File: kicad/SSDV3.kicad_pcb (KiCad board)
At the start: 4 copper layers, 58.4 x 28.8 mm, 54 parts, among them J1 XT30PW-M, J2 XT30PW-F, J3 SolderPad_1x02, J4 SolderPad_1x03, Q1 CSD19537Q3, Q2 BSZ096N10LS5, U1 LM5146

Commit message: FET Optimizations
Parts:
- removed G*** (x2): LOGO, LOGO
- added C19: 22uF, Capacitor_SMD:C_1206_3216Metric, F.Cu at (149.1, 103.6)
- added C20: 22uF, Capacitor_SMD:C_1206_3216Metric, F.Cu at (146.7, 103.6)
- added C21: 22uF, Capacitor_SMD:C_1206_3216Metric, F.Cu at (144.3, 103.6)
- added C22: 22uF, Capacitor_SMD:C_1206_3216Metric, F.Cu at (141.9, 103.6)
- added C23: 22uF, Capacitor_SMD:C_1206_3216Metric, F.Cu at (139.5, 103.6)
- added C24: 100uF, Capacitor_Tantalum_SMD:CP_EIA-7343-20_Kemet-V_HandSolder, F.Cu at (135.5, 111.5)
- added HS1: 241802B92200G, Heatsink_JJ:24180xB9x200G, B.Cu at (155.5, 111.5)
- added SW1: SW_SP3T, Button_Switch_SMD:SW_SP3T_PCM13, F.Cu at (171.0, 128.0)
- C1: value 100nF -> 100uF; footprint Capacitor_SMD:C_0603_1608Metric -> Connector_Wire:SolderWire-0.5sqmm_1x02_P4.6mm_D0.9mm_OD2.1mm
- C10, C11: value 2.2nF -> 100nF
- C12: value 10pF -> 2.2uF; footprint Capacitor_SMD:C_0603_1608Metric -> Capacitor_SMD:C_0805_2012Metric
- C13: value 22uF -> 47nF; footprint Capacitor_SMD:C_1210_3225Metric -> Capacitor_SMD:C_0603_1608Metric
- C14, C15: value 22uF -> 2.2nF; footprint Capacitor_SMD:C_1210_3225Metric -> Capacitor_SMD:C_0603_1608Metric
- C16: value 22uF -> 10pF; footprint Capacitor_SMD:C_1210_3225Metric -> Capacitor_SMD:C_0603_1608Metric
- C17: value 100uF -> 100nF; footprint Capacitor_Tantalum_SMD:CP_EIA-7343-20_Kemet-V_HandSolder -> Capacitor_SMD:C_0603_1608Metric
- C18: value 100uF -> 12pF; footprint Capacitor_Tantalum_SMD:CP_EIA-7343-20_Kemet-V_HandSolder -> Capacitor_SMD:C_0603_1608Metric
- C2: value 10uF -> 100nF; footprint Capacitor_SMD:C_1210_3225Metric -> Capacitor_SMD:C_0603_1608Metric
- C3, C4: value 10uF -> 4.7uF; footprint Capacitor_SMD:C_1210_3225Metric -> Capacitor_SMD:C_1206_3216Metric
- C5, C8: value 100nF -> 4.7uF; footprint Capacitor_SMD:C_0603_1608Metric -> Capacitor_SMD:C_1206_3216Metric
- C6: value 2.2uF -> 4.7uF; footprint Capacitor_SMD:C_0805_2012Metric -> Capacitor_SMD:C_1206_3216Metric
- C7: value 47nF -> 4.7uF; footprint Capacitor_SMD:C_0603_1608Metric -> Capacitor_SMD:C_1206_3216Metric
- C9: value 12pF -> 100nF
- D1: value 1.5SMCxxA -> SMBJ64A; footprint Diode_SMD:D_SMC -> Diode_SMD:D_SMB; moved to F.Cu
- J1: value XT30PW-M -> XT30U-M; footprint Connector_AMASS:AMASS_XT30PW-M_1x02_P2.50mm_Horizontal -> Connector_AMASS:AMASS_XT30U-M_1x02_P5.0mm_Vertical; moved to B.Cu
- J2: value XT30PW-F -> XT30U-F; footprint Connector_AMASS:AMASS_XT30PW-F_1x02_P2.50mm_Horizontal -> Connector_AMASS:AMASS_XT30U-F_1x02_P5.0mm_Vertical; moved to B.Cu
- J3: value SolderPad_1x02 -> Conn_01x02_MountingPin; footprint Connector_Pad:SolderWirePad_1x02_SMD_1.5x2mm -> Connector_JST:JST_GH_SM02B-GHS-TB_1x02-1MP_P1.25mm_Horizontal; moved to F.Cu
- J4: value SolderPad_1x03 -> Conn_01x03_MountingPin; footprint Connector_Pad:SolderWirePad_1x03_SMD_1.5x2mm -> Connector_JST:JST_GH_SM03B-GHS-TB_1x03-1MP_P1.25mm_Horizontal
- JP1, JP2: moved to F.Cu
- L1: value 6.8uH -> 4.7uH; footprint Inductor_SMD:L_Vishay_IHLP-4040 -> Inductor_SMD:L_Bourns_SRP1038C_10.0x10.0mm
- Q1: value CSD19537Q3 -> BSZ146N10LS5ATMA1; footprint Package_SON_JJ:Texas_DQG0008A_3.3x3.3mm_P0.65mm_ThermalVias-D0.3mm -> Package_SON_JJ:Infineon_PG-TSDSON-8-26_3.3x3.3mm_P0.65mm_ThermalVias-D0.3mm
- Q2: value BSZ096N10LS5 -> BSZ146N10LS5ATMA1; footprint Package_SON_JJ:Infineon_PG-TSDSON-8-26_3.3x3.3mm_P0.65mm_ThermalVias-D0.3mm -> Package_SON_JJ:Infineon_PG-TSDSON-8-26_3.3x3.3mm_P0.65mm
- R1: value 150k -> 2.2
- R10: value 1k -> 6.8k
- R11: value 20k -> 6.81k
- R12: value 15k -> 3.48k
- R13: value 6.81k -> 3.74k
- R14: value 3.48k -> 2.2
- R15: value 3.74k -> 430
- R2: value 13k -> 150k
- R3: value 2.2 -> 13k
- R4: value 33k -> 20k
- R5: value 20k -> 24k
- R6: value 0 -> 20k
- R7: value 20k -> 0
- R8: value 2.2 -> 1k
- R9: value 430 -> 20k
- moved JP1 85.3 mm to (75.8, 142.3), turned to 0 degrees
- moved J4 84.1 mm to (78.3, 109.1)
- moved JP2 83.1 mm to (75.8, 145.8), turned to 0 degrees
- moved H2 79.8 mm to (92.2, 109.1), turned to 0 degrees
- moved H3 78.3 mm to (92.2, 111.5), turned to 0 degrees
- moved D3 63.1 mm to (101.7, 107.8)
- moved C1 57.5 mm to (99.5, 146.2), turned to 0 degrees
- moved D4 52.5 mm to (96.3, 107.1), turned to 0 degrees
- moved NT1 47.9 mm to (107.6, 130.4), turned to 0 degrees
- moved J3 44.6 mm to (187.8, 103.5), turned to 90 degrees
- moved R16 44.1 mm to (108.5, 128.2)
- moved D2 43.5 mm to (108.6, 125.2), turned to 0 degrees
- moved H1 36.0 mm to (92.2, 106.6), turned to 0 degrees
- moved C14 33.7 mm to (170.0, 113.8), turned to 180 degrees
- moved C16 29.9 mm to (165.8, 116.2), turned to -90 degrees
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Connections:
- C1 pad 1: /buck_converter/U1_VIN -> VIN
- C10 pad 1: /buck_converter/COMP_RC2 -> VIN
- C10 pad 2: /buck_converter/FB -> PGND
- C11 pad 1: /buck_converter/COMP -> VIN
- C11 pad 2: /buck_converter/COMP_RC1 -> PGND
- C12 pad 1: /buck_converter/FB -> VCC
- C12 pad 2: /buck_converter/COMP -> PGND
- C13 pad 1: VOUT -> /buck_converter/SS_TRK
- C13 pad 2: PGND -> AGND
- C14 pad 1: VOUT -> /buck_converter/COMP_RC2
- C14 pad 2: PGND -> /buck_converter/FB
- C15 pad 1: VOUT -> /buck_converter/COMP
- C15 pad 2: PGND -> /buck_converter/COMP_RC1
- C16 pad 1: VOUT -> /buck_converter/FB
- C16 pad 2: PGND -> /buck_converter/COMP
- C17 pad 1: VOUT -> /buck_converter/RBST
- C17 pad 2: PGND -> /buck_converter/BST
- C18 pad 1: VOUT -> /buck_converter/ILIM
- C2 pad 1: VIN -> /buck_converter/U1_VIN
- C6 pad 1: VCC -> VIN
- C7 pad 1: /buck_converter/SS_TRK -> VIN
- C7 pad 2: AGND -> PGND
- C8 pad 1: /buck_converter/RBST -> VIN
- C8 pad 2: /buck_converter/BST -> PGND
- C9 pad 1: /buck_converter/ILIM -> VIN
- Q1 pad 2: /buck_converter/SW -> /buck_converter/HO
- Q1 pad 3: /buck_converter/SW -> VIN
- R1 pad 2: U1_EN -> /buck_converter/U1_VIN
- R10 pad 1: VOUT -> /buck_converter/FB
- R10 pad 2: /buck_converter/COMP_RC2 -> /buck_converter/COMP_RC1
- R11 pad 1: VOUT -> /buck_converter/FB
- R11 pad 2: /buck_converter/FB -> /buck_converter/JP_CFG1
- R12 pad 2: /buck_converter/COMP_RC1 -> /buck_converter/JP_CFG2
- R13 pad 2: /buck_converter/JP_CFG1 -> AGND
- R14 pad 1: /buck_converter/FB -> /buck_converter/RBST
- R14 pad 2: /buck_converter/JP_CFG2 -> /buck_converter/SW
- R15 pad 1: /buck_converter/FB -> /buck_converter/SW
- R15 pad 2: AGND -> /buck_converter/ILIM
- R2 pad 1: U1_EN -> VIN
- R2 pad 2: AGND -> U1_EN
- R3 pad 1: VIN -> U1_EN
- R3 pad 2: /buck_converter/U1_VIN -> AGND
- R4 pad 1: /buck_converter/RT -> VCC
- R4 pad 2: AGND -> PG
- R5 pad 1: VCC -> /buck_converter/RT
- R5 pad 2: /buck_converter/SYNCIN -> AGND
- R6 pad 1: /buck_converter/SYNCIN -> VCC
- R6 pad 2: AGND -> /buck_converter/SYNCIN
- R7 pad 1: VCC -> /buck_converter/SYNCIN
- R7 pad 2: PG -> AGND
- R8 pad 1: /buck_converter/RBST -> VOUT
- R8 pad 2: /buck_converter/SW -> /buck_converter/COMP_RC2
- R9 pad 1: /buck_converter/SW -> VOUT
- R9 pad 2: /buck_converter/ILIM -> /buck_converter/FB
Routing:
- net PGND: track 25.1 -> 0.00 mm, vias 78 -> 0
- net U1_EN: track 19.1 -> 0.00 mm, vias 1 -> 0
- net VIN: track 17.5 -> 0.00 mm, vias 12 -> 0
- net VCC: track 17.1 -> 0.00 mm, vias 2 -> 0
- net AGND: track 16.6 -> 0.00 mm, vias 2 -> 0
- net /buck_converter/SW: track 19.4 -> 3.11 mm, vias 4 -> 1
- net /buck_converter/FB: track 15.6 -> 0.00 mm
- net /buck_converter/LO: track 15.0 -> 0.00 mm, vias 2 -> 0
- net PG: track 11.3 -> 0.00 mm
- net /buck_converter/COMP: track 5.55 -> 0.00 mm
- net /buck_converter/HO: track 6.61 -> 1.38 mm, vias 2 -> 1
- net /buck_converter/SYNCIN: track 4.41 -> 0.00 mm
- net VOUT: track 4.05 -> 0.00 mm, vias 1 -> 0
- net /buck_converter/U1_VIN: track 2.97 -> 0.00 mm
- net /buck_converter/ILIM: track 2.92 -> 0.00 mm
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- removed copper zone on F.Cu, net /buck_converter/HO
- removed copper zone on F.Cu, net /buck_converter/LO
- removed copper zone on B.Cu, net /buck_converter/SW
- removed copper zone on F.Cu, net /buck_converter/SW
- removed copper zone on In2.Cu, net /buck_converter/SW
- removed copper zone on F.Cu, net /buck_converter/U1_VIN
- removed copper zone on F.Cu, net AGND
- removed copper zone on B.Cu, net PGND
- removed copper zone on F.Cu, net PGND
- removed copper zone on In2.Cu, net PGND
- removed copper zone on B.Cu, net VIN
- removed copper zone on F.Cu, net VIN
- removed copper zone on In2.Cu, net VIN
- removed copper zone on B.Cu, net VOUT
- removed copper zone on F.Cu, net VOUT
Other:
- board size 58.4 x 28.8 mm -> 71 x 23 mm
- board text removed: "12V"
- board text removed: "5.1V"
- board text removed: "7.4V"
- board text removed: "9.6V"
- board text removed: "CAUTION HOT SURFACE"
- board text removed: "EN"
- board text removed: "GND"
- board text removed: "INPUT: 20-60V⎓4A OUTPUT: 5.1-12V⎓8A"
- board text removed: "JLCJLCJLCJLC"
- board text removed: "OFF"
- board text removed: "ON"
- board text removed: "OUTPUT CONFIG"
- board text removed: "PG"
- board text removed: "Prod 2545 Rev. D"
- board text removed: "Prod 2545 Rev. D Julian Joaquin"
- board text removed: "SSD"
- board text removed: "V1"
- board text removed: "V2"
- board text removed: "V3"
- board text removed: "VCC"

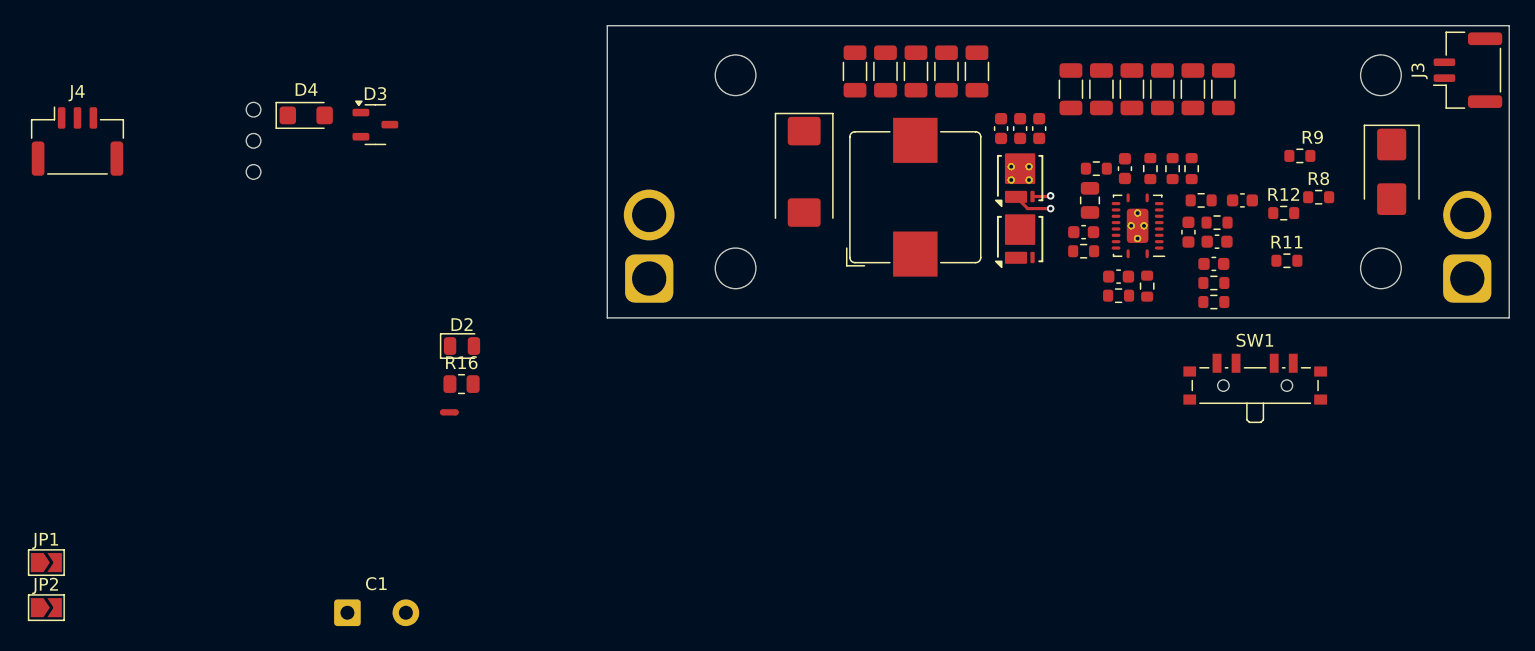
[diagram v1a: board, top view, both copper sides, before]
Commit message: Wrong design files initially commited
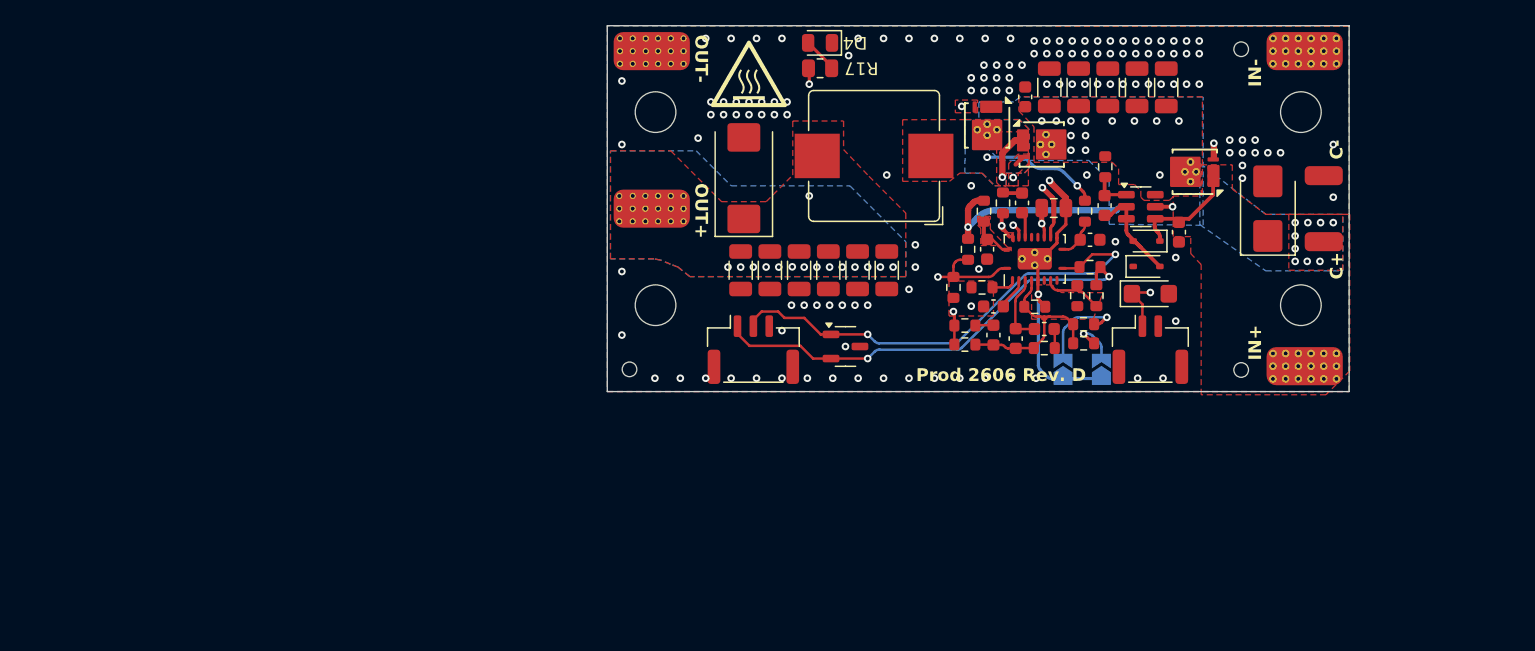
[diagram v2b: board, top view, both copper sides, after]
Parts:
- removed C1: 100uF, Connector_Wire:SolderWire-0.5sqmm_1x02_P4.6mm_D0.9mm_OD2.1mm
- removed SW1: SW_SP3T, Button_Switch_SMD:SW_SP3T_PCM13
- added D5: 60V, Diode_SMD:D_SMF, F.Cu at (162.8, 121.1)
- added D6: 8V, Package_TO_SOT_SMD:SOT-23-3, F.Cu at (138.8, 125.2)
- added G***: LOGO, LOGO, F.Cu at (131.1, 103.8)
- added G***: LOGO, LOGO, B.Cu at (146.5, 119.0)
- added J5: SolderPad, Connector_Wire:SolderWirePad_1x01_SMD_3x6mm, F.Cu at (123.5, 114.4)
- added J6: SolderPad, Connector_Wire:SolderWirePad_1x01_SMD_3x6mm, F.Cu at (123.5, 102.0)
- added J7: SM02B-GHS-TB(LF)(SN), Connector_JST:JST_GH_SM02B-GHS-TB_1x02-1MP_P1.25mm_Horizontal, F.Cu at (162.8, 125.5)
- added J8: SM03B-GHS-TB(LF)(SN), Connector_JST:JST_GH_SM03B-GHS-TB_1x03-1MP_P1.25mm_Horizontal, F.Cu at (131.5, 125.5)
- added Q3: BSZ146N10LS5, Package_SON_JJ:Infineon_PG-TSDSON-8-26_3.3x3.3mm_P0.65mm_ThermalVias-D0.3mm, F.Cu at (149.9, 107.8)
- added R17: 1k, Resistor_SMD:R_0805_2012Metric, F.Cu at (136.7, 103.3)
- added U2: LM5146, Package_QFN_JJ:Texas_RGY0020B_EP_3.5x4.5mm_P0.5mm_ThermalVias-D0.3mm, F.Cu at (153.6, 118.3)
- C11: value 100nF -> 2.2uF; footprint Capacitor_SMD:C_0603_1608Metric -> Capacitor_SMD:C_0805_2012Metric
- C12: value 2.2uF -> 47nF; footprint Capacitor_SMD:C_0805_2012Metric -> Capacitor_SMD:C_0603_1608Metric
- C13: value 47nF -> 100nF
- C14: value 2.2nF -> 8.2pF
- C15: value 2.2nF -> 1.5nF
- C16: value 10pF -> 4.7nF
- C17: value 100nF -> 68pF
- C18: value 12pF -> 22uF; footprint Capacitor_SMD:C_0603_1608Metric -> Capacitor_SMD:C_1206_3216Metric
- C3, C4: value 4.7uF -> 100nF; footprint Capacitor_SMD:C_1206_3216Metric -> Capacitor_SMD:C_0603_1608Metric
- C9: value 100nF -> 4.7uF; footprint Capacitor_SMD:C_0603_1608Metric -> Capacitor_SMD:C_1206_3216Metric
- D1: value SMBJ64A -> 64V
- D2: value GREEN -> BAT46WS; footprint LED_SMD:LED_0805_2012Metric -> Diode_SMD:D_SOD-323
- D3: value 8V -> BAT46WS; footprint Package_TO_SOT_SMD:SOT-23-3 -> Diode_SMD:D_SOD-323
- D4: value 60V -> GREEN; footprint Diode_SMD:D_SMF -> LED_SMD:LED_0805_2012Metric
- J1: value XT30U-M -> SolderPad; footprint Connector_AMASS:AMASS_XT30U-M_1x02_P5.0mm_Vertical -> Connector_Wire:SolderWirePad_1x01_SMD_3x6mm; moved to F.Cu
- J2: value XT30U-F -> SolderPad; footprint Connector_AMASS:AMASS_XT30U-F_1x02_P5.0mm_Vertical -> Connector_Wire:SolderWirePad_1x01_SMD_1.5x3mm; moved to F.Cu
- J3: value Conn_01x02_MountingPin -> SolderPad; footprint Connector_JST:JST_GH_SM02B-GHS-TB_1x02-1MP_P1.25mm_Horizontal -> Connector_Wire:SolderWirePad_1x01_SMD_1.5x3mm
- J4: value Conn_01x03_MountingPin -> SolderPad; footprint Connector_JST:JST_GH_SM03B-GHS-TB_1x03-1MP_P1.25mm_Horizontal -> Connector_Wire:SolderWirePad_1x01_SMD_3x6mm
- JP1, JP2: moved to B.Cu
- Q1: value BSZ146N10LS5ATMA1 -> BSZ146N10LS5
- Q2: value BSZ146N10LS5ATMA1 -> BSZ146N10LS5; footprint Package_SON_JJ:Infineon_PG-TSDSON-8-26_3.3x3.3mm_P0.65mm -> Package_SON_JJ:Infineon_PG-TSDSON-8-26_3.3x3.3mm_P0.65mm_ThermalVias-D0.3mm
- R1: value 2.2 -> 1.5k
- R10: value 6.8k -> 560
- R11: value 6.81k -> 1.5k
- R12: value 3.48k -> 20k
- R13: value 3.74k -> 10k
- R14: value 2.2 -> 6.81k
- R15: value 430 -> 3.48k
- R16: value 1k -> 3.74k; footprint Resistor_SMD:R_0805_2012Metric -> Resistor_SMD:R_0603_1608Metric
- R3: value 13k -> 12k
- R4, R9: value 20k -> 2.2
- R8: value 1k -> 20k
- U1: value LM5146 -> LM5050-1; footprint Package_QFN_JJ:Texas_RGY0020B_EP_3.5x4.5mm_P0.5mm_ThermalVias-D0.3mm -> Package_TO_SOT_SMD:TSOT-23-6
- moved J4 96.9 mm to (174.9, 102.0), turned to -90 degrees
- moved JP2 85.1 mm to (158.9, 127.0), turned to 90 degrees
- moved JP1 81.5 mm to (155.9, 127.0), turned to 90 degrees
- moved H2 79.8 mm to (169.9, 127.1), turned to 180 degrees
- moved H3 78.3 mm to (169.9, 101.8), turned to 180 degrees
- moved D3 61.7 mm to (162.4, 119.0)
- moved D2 54.5 mm to (162.4, 117.0), turned to 180 degrees
- moved J2 53.2 mm to (176.4, 117.0), turned to -90 degrees
- moved NT1 47.6 mm to (153.9, 119.4), turned to -90 degrees
- moved R16 45.5 mm to (153.6, 122.1)
- moved D4 40.9 mm to (136.7, 101.3), turned to 180 degrees
- moved H1 36.0 mm to (121.8, 127.0), turned to 180 degrees
- moved R12 27.2 mm to (148.1, 125.1)
- moved R11 25.9 mm to (148.1, 123.6)
- moved R9 23.7 mm to (151.1, 114.0), turned to -90 degrees
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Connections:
- C11 pad 1: VIN -> VCC
- C12 pad 1: VCC -> /buck_converter/SS_TRK
- C12 pad 2: PGND -> AGND
- C13 pad 1: /buck_converter/SS_TRK -> /buck_converter/RBST
- C13 pad 2: AGND -> /buck_converter/BST
- C14 pad 1: /buck_converter/COMP_RC2 -> /buck_converter/ILIM
- C14 pad 2: /buck_converter/FB -> PGND
- C15 pad 1: /buck_converter/COMP -> /buck_converter/COMP_RC2
- C15 pad 2: /buck_converter/COMP_RC1 -> /buck_converter/FB
- C16 pad 1: /buck_converter/FB -> /buck_converter/COMP
- C16 pad 2: /buck_converter/COMP -> /buck_converter/COMP_RC1
- C17 pad 1: /buck_converter/RBST -> /buck_converter/FB
- C17 pad 2: /buck_converter/BST -> /buck_converter/COMP
- C18 pad 1: /buck_converter/ILIM -> VOUT
- C2 pad 1: /buck_converter/U1_VIN -> VBAT
- C3 pad 1: VIN -> /rpp/U1_VS
- C3 pad 2: PGND -> /rpp/U1_GND
- C4 pad 1: VIN -> /buck_converter/U2_VIN
- D1 pad 1: VIN -> VBAT
- D2 pad 1: PGND -> VBAT
- D2 pad 2: /buck_converter/VOUT_LED -> /rpp/U1_GND
- D3 pad 1: PG -> PGND
- D3 pad 2: VCC -> /rpp/U1_GND
- D4 pad 1: U1_EN -> PGND
- D4 pad 2: PGND -> /buck_converter/VOUT_LED
- J1 pad 1: PGND -> VBAT
- J2 pad 1: PGND -> VIN
- J3 pad 1: U1_EN -> PGND
- J4 pad 1: VCC -> PGND
- Q1 pad 1: /buck_converter/SW -> VBAT
- Q1 pad 2: /buck_converter/HO -> /rpp/U1_GATE
- Q2 pad 1: PGND -> /buck_converter/SW
- Q2 pad 2: /buck_converter/LO -> /buck_converter/HO
- Q2 pad 3: /buck_converter/SW -> VIN
- R1 pad 2: /buck_converter/U1_VIN -> /rpp/U1_VS
- R10 pad 1: /buck_converter/FB -> /buck_converter/SW
- R10 pad 2: /buck_converter/COMP_RC1 -> /buck_converter/ILIM
- R11 pad 1: /buck_converter/FB -> VOUT
- R11 pad 2: /buck_converter/JP_CFG1 -> /buck_converter/COMP_RC2
- R12 pad 1: /buck_converter/FB -> VOUT
- R12 pad 2: /buck_converter/JP_CFG2 -> /buck_converter/FB
- R13 pad 2: AGND -> /buck_converter/COMP_RC1
- R14 pad 1: /buck_converter/RBST -> /buck_converter/FB
- R14 pad 2: /buck_converter/SW -> /buck_converter/JP_CFG1
- R15 pad 1: /buck_converter/SW -> /buck_converter/FB
- R15 pad 2: /buck_converter/ILIM -> /buck_converter/JP_CFG2
- R16 pad 1: VOUT -> /buck_converter/FB
- R16 pad 2: /buck_converter/VOUT_LED -> AGND
- R2 pad 2: U1_EN -> U2_EN
- R3 pad 1: U1_EN -> U2_EN
- R4 pad 1: VCC -> VIN
- R4 pad 2: PG -> /buck_converter/U2_VIN
- R8 pad 1: VOUT -> VCC
- R8 pad 2: /buck_converter/COMP_RC2 -> PG
- R9 pad 1: VOUT -> /buck_converter/RBST
- R9 pad 2: /buck_converter/FB -> /buck_converter/SW
- U1 pad 1: U1_EN -> /rpp/U1_VS
- U1 pad 2: /buck_converter/RT -> /rpp/U1_GND
- U1 pad 3: /buck_converter/SS_TRK -> /rpp/U1_GND
- U1 pad 4: /buck_converter/COMP -> VBAT
- U1 pad 5: /buck_converter/FB -> /rpp/U1_GATE
- U1 pad 6: AGND -> VIN
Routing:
- net VCC: track 0.00 -> 44.9 mm, vias 0 -> 3
- net VOUT: track 0.00 -> 38.7 mm, vias 0 -> 17
- net PG: track 0.00 -> 37.6 mm, vias 0 -> 2
- net U2_EN: track 0.00 -> 29.4 mm, vias 0 -> 2
- net AGND: track 0.00 -> 19.1 mm, vias 0 -> 2
- net PGND: track 0.00 -> 18.2 mm, vias 0 -> 134
- net /buck_converter/SW: track 3.11 -> 19.3 mm, vias 1 -> 4
- net VIN: track 0.00 -> 16.2 mm, vias 0 -> 23
- net /buck_converter/FB: track 0.00 -> 15.6 mm
- net /buck_converter/LO: track 0.00 -> 15.0 mm, vias 0 -> 2
- net /rpp/U1_GATE: track 0.00 -> 9.31 mm, vias 0 -> 2
- net /rpp/U1_GND: track 0.00 -> 8.09 mm
- net VBAT: track 0.00 -> 7.80 mm
- net /buck_converter/JP_CFG1: track 0.00 -> 7.09 mm, vias 0 -> 1
- net /buck_converter/COMP: track 0.00 -> 5.55 mm
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- added copper zone on F.Cu, net /buck_converter/HO
- added copper zone on F.Cu, net /buck_converter/LO
- added copper zone on B.Cu, net /buck_converter/SW
- added copper zone on F.Cu, net /buck_converter/SW
- added copper zone on In2.Cu, net /buck_converter/SW
- added copper zone on F.Cu, net /buck_converter/U2_VIN
- added copper zone on F.Cu, net AGND
- added copper zone on B.Cu, net PGND
- added copper zone on F.Cu, net PGND
- added copper zone on In2.Cu, net PGND
- added copper zone on F.Cu, net VBAT
- added copper zone on B.Cu, net VIN
- added copper zone on F.Cu, net VIN
- added copper zone on In1.Cu, net VIN
- added copper zone on In2.Cu, net VIN
- added copper zone on B.Cu, net VOUT
- added copper zone on F.Cu, net VOUT
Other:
- board size 71 x 23 mm -> 58.4 x 28.8 mm
- board text added: "12V"
- board text added: "5.1V"
- board text added: "7.4V"
- board text added: "9.6V"
- board text added: "C+"
- board text added: "C-"
- board text added: "CAUTION HOT SURFACE"
- board text added: "EN"
- board text added: "GND"
- board text added: "IN+"
- board text added: "IN-"
- board text added: "INPUT: 20-60V⎓3A OUTPUT: 5.1-12V⎓8A"
- board text added: "JLCJLCJLCJLC"
- board text added: "OFF"
- board text added: "ON"
- board text added: "OUT+"
- board text added: "OUT-"
- board text added: "OUTPUT CONFIG"
- board text added: "PG"
- board text added: "Prod 2606 Rev. D"
- board text added: "Prod 2606 Rev. D Julian Joaquin"
- board text added: "SSD"
- board text added: "V1"
- board text added: "V2"
- board text added: "V3"
- board text added: "VCC"
